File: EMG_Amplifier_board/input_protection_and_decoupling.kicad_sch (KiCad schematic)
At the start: 9 parts, among them U7 TPD2E001DRLR

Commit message: add footprints
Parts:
- D1, D2: footprint (none) -> Diode_SMD:D_SOD-523
- L1, L2: footprint (none) -> BLM15AX102SN1D_footprints:IND_BLM15_1P05X0P55X0P55_MUR
- R1, R2: footprint (none) -> Resistor_SMD:R_0805_2012Metric
- R3, R4: footprint (none) -> Resistor_SMD:R_0603_1608Metric
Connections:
- net GND: now also U7.1 (VCC), U7.2 (NC)

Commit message: acomponents choice
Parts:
- R1, R2: footprint Resistor_SMD:R_0805_2012Metric -> Resistor_SMD:R_01005_0402Metric
- R3, R4: footprint Resistor_SMD:R_0603_1608Metric -> Resistor_SMD:R_0402_1005Metric
- U7: footprint DRL5 -> TPD2E001DRLR_footprints:DRL5-L
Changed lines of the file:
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@@
 			)
 		)
-		(property "Footprint" "Resistor_SMD:R_0603_1608Metric"
+		(property "Footprint" "Resistor_SMD:R_0402_1005Metric"
 			(at 114.3 113.538 90)
 			(effects
@@
 			)
 		)
-		(property "Footprint" "Resistor_SMD:R_0603_1608Metric"
+		(property "Footprint" "Resistor_SMD:R_0402_1005Metric"
 			(at 114.3 76.708 90)
 			(effects
@@
 			)
 		)
-		(property "Footprint" "DRL5"
+		(property "Footprint" "TPD2E001DRLR_footprints:DRL5-L"
 			(at 68.58 90.17 0)
 			(effects
@@
 			)
 		)
-		(property "Footprint" "Resistor_SMD:R_0805_2012Metric"
+		(property "Footprint" "Resistor_SMD:R_01005_0402Metric"
 			(at 67.31 113.538 90)
 			(effects
@@
 			)
 		)
-		(property "Footprint" "Resistor_SMD:R_0805_2012Metric"
+		(property "Footprint" "Resistor_SMD:R_01005_0402Metric"
 			(at 67.31 76.708 90)
 			(effects

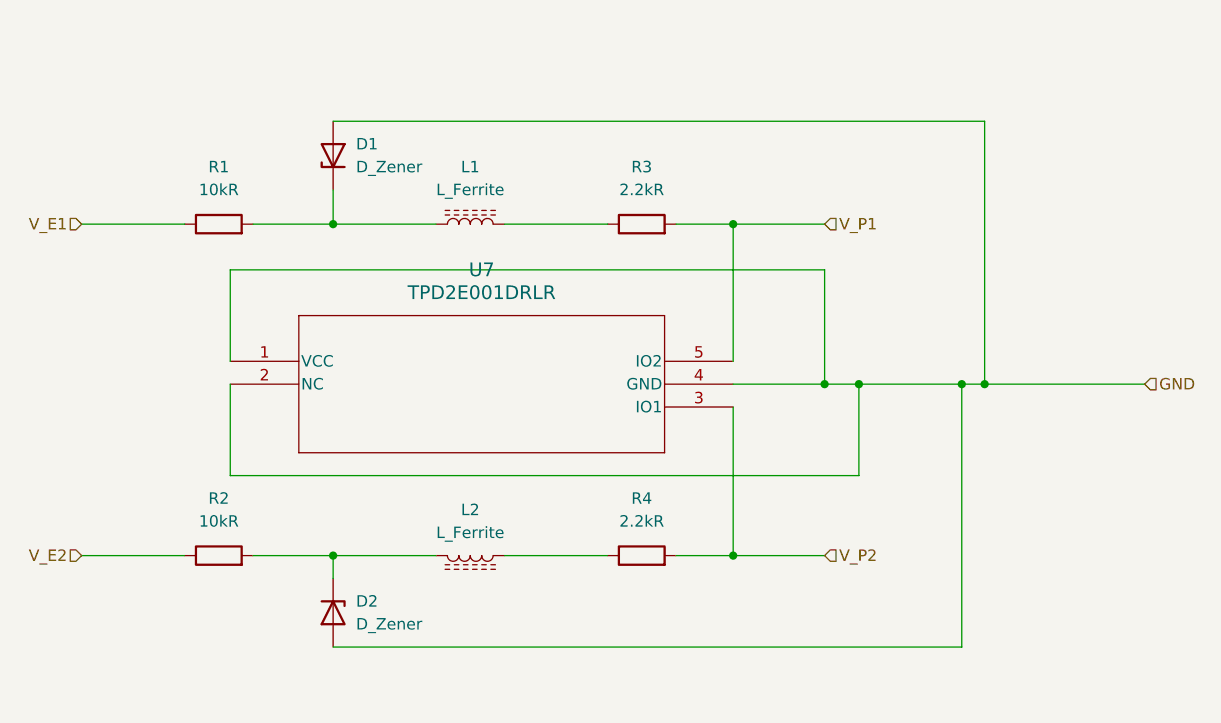
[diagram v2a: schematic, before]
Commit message: update the schematic with shared grounds and pin connectors
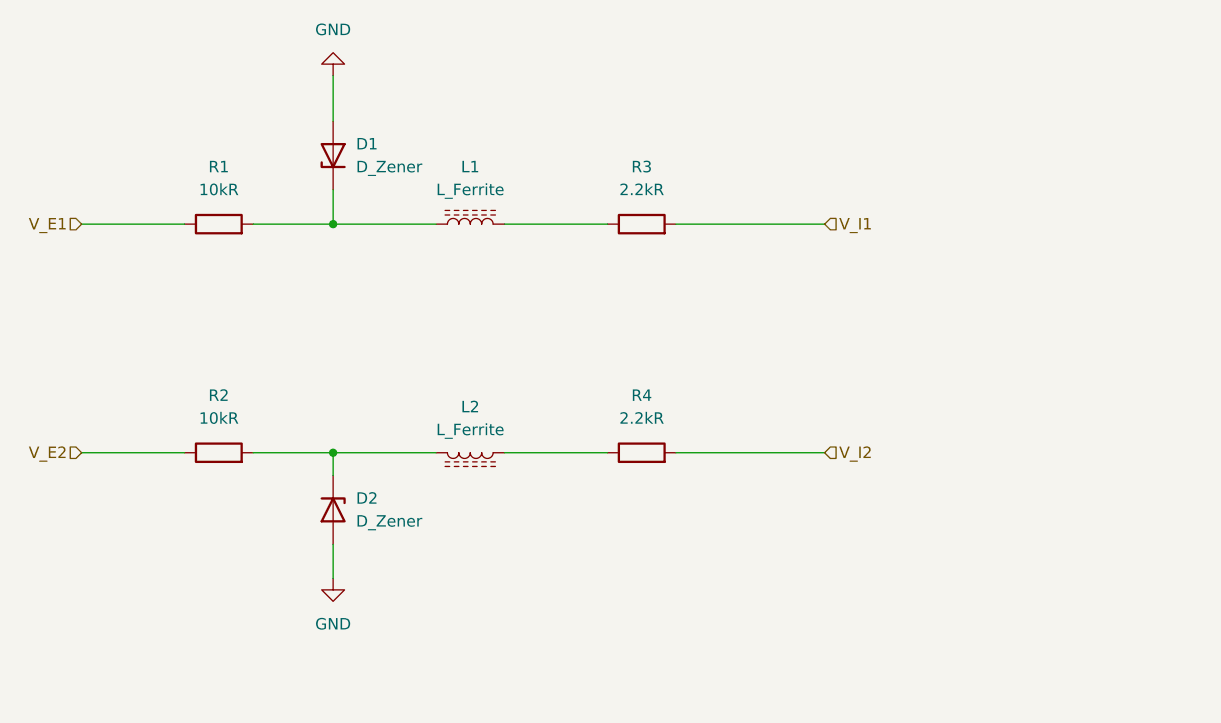
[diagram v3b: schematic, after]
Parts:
- removed U7: TPD2E001DRLR, TPD2E001DRLR_footprints:DRL5-L, symbol TPD2E001:TPD2E001DRLR
- R1, R2: footprint Resistor_SMD:R_01005_0402Metric -> Resistor_SMD:R_0402_1005Metric
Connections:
- net V_P1 renamed V_I1
- net V_P2 renamed V_I2
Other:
- moved on the sheet: D2, L2, R2, R4

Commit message: first revision
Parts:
- R1, R2: value 10kR -> 10k
- R3, R4: value 2.2kR -> 2.2k
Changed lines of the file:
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@@
 			)
 		)
-		(property "Value" "2.2kR"
+		(property "Value" "2.2k"
 			(at 114.3 96.52 90)
 			(effects
@@
 			)
 		)
-		(property "Value" "2.2kR"
+		(property "Value" "2.2k"
 			(at 114.3 71.12 90)
 			(effects
@@
 			)
 		)
-		(property "Value" "10kR"
+		(property "Value" "10k"
 			(at 67.31 96.52 90)
 			(effects
@@
 			)
 		)
-		(property "Value" "10kR"
+		(property "Value" "10k"
 			(at 67.31 71.12 90)
 			(effects
